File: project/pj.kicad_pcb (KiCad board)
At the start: 2 copper layers, 65 x 56.5 mm, 19 parts, among them J1 RPi_GPIO, J10 Pico PWR enable, J12 Conn_01x16_Pin, J2 2B+, J3 zero, J4 3A+, J5 3B+, J6 4, J7 Conn_01x02, J8 Conn_01x02, J9 External PWR, SW1 SW_Push, SW2 SW_Push

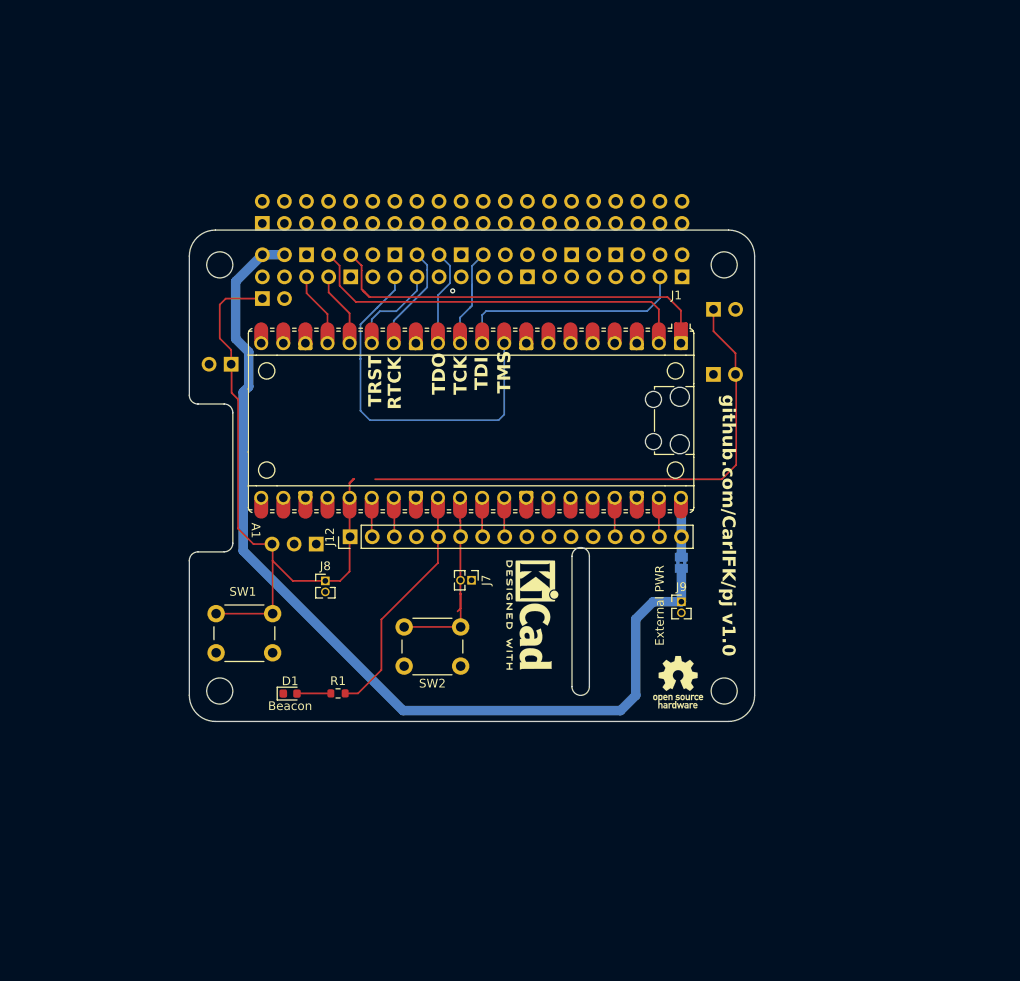
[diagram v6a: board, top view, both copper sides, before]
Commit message: ground plane, reroute some reset
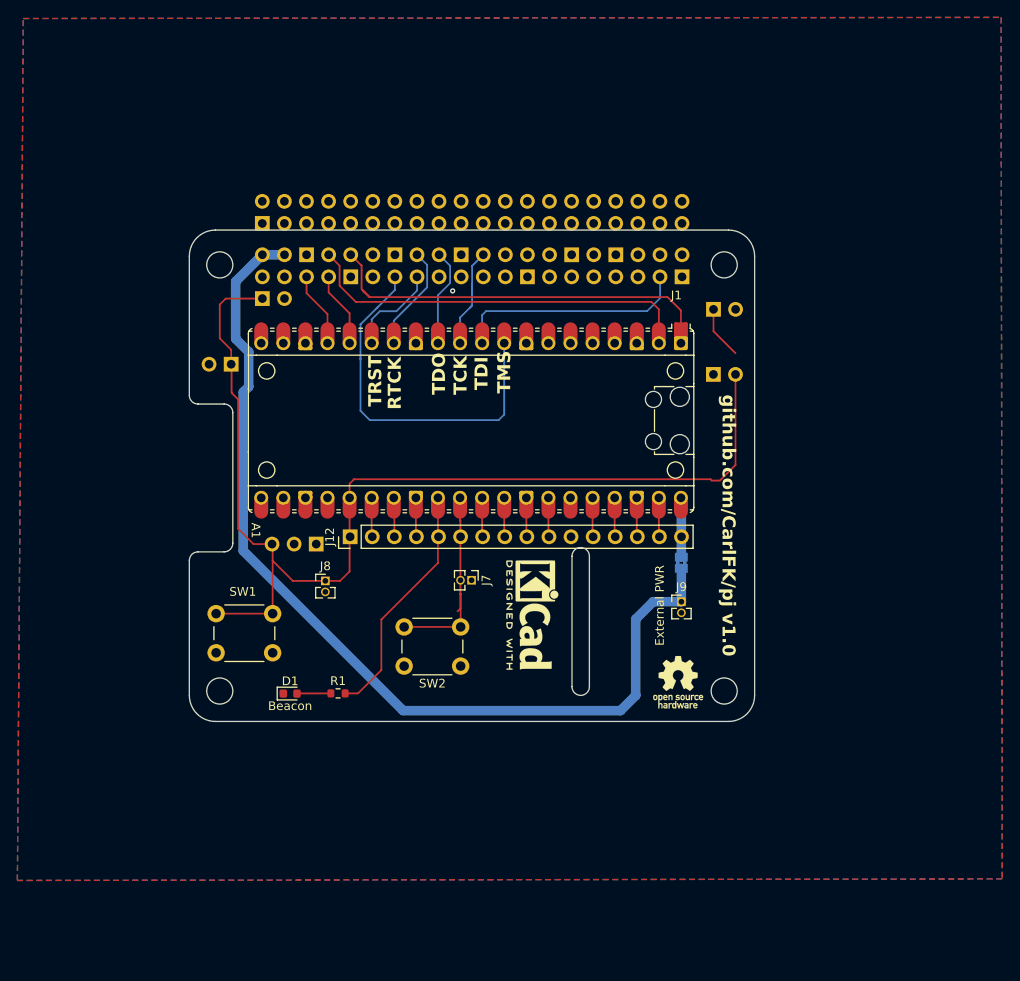
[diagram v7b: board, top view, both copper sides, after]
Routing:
- net unconnected-(J4-Pin_1-Pad1): track 61.1 -> 6.10 mm
- net Net-(A1-GPIO19): track 72.8 -> 127.1 mm
- net GND: track 0.19 -> 9.20 mm
- net Net-(A1-GPIO28_ADC2): track 0.00 -> 4.51 mm
- net Net-(A1-AGND): track 0.00 -> 4.51 mm
- net Net-(A1-3V3): track 0.00 -> 4.51 mm
- added copper zone on B.Cu, net GND
- added copper zone on F.Cu, net GND
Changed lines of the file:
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@@
 		(fp_arc
 			(start 10.579676 25.189937)
-			(mid 10.35796 25.493961)
+			(mid 10.357949 25.493953)
 			(end 10 25.61)
 			(stroke
@@
 		)
 		(property "Value" "3B+"
-			(at 0 -4.87 90)
-			(layer "B.Fab")
+			(at -2 -2.61 0)
+			(layer "F.Fab")
 			(effects
 				(font
@@
 					(thickness 0.15)
 				)
-				(justify mirror)
 			)
 		)
@@
 		)
 		(property "Value" "3A+"
-			(at 0 -4.87 90)
-			(layer "B.Fab")
+			(at 2 -0.13 0)
+			(layer "F.Fab")
 			(effects
 				(font
@@
 					(thickness 0.15)
 				)
-				(justify mirror)
 			)
 		)
@@
 		(net 10)
 	)
+	(segment
+		(start 62.4675 71.28)
+		(end 62.4675 75.6975)
+		(width 0.2)
+		(layer "F.Cu")
+		(net 11)
+	)
+	(segment
+		(start 62.4675 75.6975)
+		(end 62.53 75.76)
+		(width 0.2)
+		(layer "F.Cu")
+		(net 11)
+	)
+	(segment
+		(start 87.8675 75.6975)
+		(end 87.93 75.76)
+		(width 0.2)
+		(layer "F.Cu")
+		(net 11)
+	)
+	(segment
+		(start 87.8675 71.28)
+		(end 87.8675 75.6975)
+		(width 0.2)
+		(layer "F.Cu")
+		(net 11)
+	)
 	(via
 		(at 66.7 47.49)
@@
 	)
 	(segment
-		(start 44.82 48.37)
-		(end 40.61 48.37)
+		(start 96.336278 69.146278)
+		(end 55.363722 69.146278)
 		(width 0.2)
 		(layer "F.Cu")
@@
 	)
 	(segment
-		(start 42.02 74.82)
-		(end 43.8 76.6)
+		(start 44.82 48.37)
+		(end 40.61 48.37)
 		(width 0.2)
 		(layer "F.Cu")
@@
 	)
 	(segment
-		(start 54.8475 71.28)
-		(end 54.8475 69.6325)
+		(start 42.02 74.82)
+		(end 43.8 76.6)
 		(width 0.2)
 		(layer "F.Cu")
@@
 	)
 	(segment
-		(start 55.38 69.1)
-		(end 55.28 69.1)
+		(start 54.8475 69.6625)
+		(end 55.3 69.21)
 		(width 0.2)
 		(layer "F.Cu")
@@
 	)
 	(segment
-		(start 54.8475 69.6325)
-		(end 55.38 69.1)
+		(start 99.22 57.09)
+		(end 99.22 67.51)
 		(width 0.2)
 		(layer "F.Cu")
@@
 	)
 	(segment
+		(start 54.8475 71.28)
+		(end 54.8475 69.6625)
+		(width 0.2)
+		(layer "F.Cu")
+		(net 13)
+	)
+	(segment
 		(start 46 76.67)
 		(end 45.93 76.6)
@@
 	)
 	(segment
+		(start 99.22 67.51)
+		(end 97.43 69.3)
+		(width 0.2)
+		(layer "F.Cu")
+		(net 13)
+	)
+	(segment
+		(start 55.363722 69.146278)
+		(end 55.3 69.21)
+		(width 0.2)
+		(layer "F.Cu")
+		(net 13)
+	)
+	(segment
 		(start 52.06 79.18)
 		(end 52.11 79.13)
@@
 	)
 	(segment
-		(start 55.28 69.1)
-		(end 54.81 69.57)
+		(start 96.49 69.3)
+		(end 96.336278 69.146278)
 		(width 0.2)
 		(layer "F.Cu")
@@
 	)
 	(segment
+		(start 97.43 69.3)
+		(end 96.49 69.3)
+		(width 0.2)
+		(layer "F.Cu")
+		(net 13)
+	)
+	(segment
 		(start 46 78.51)
 		(end 46 76.67)
@@
 	)
 	(segment
+		(start 82.7875 75.6975)
+		(end 82.85 75.76)
+		(width 0.2)
+		(layer "F.Cu")
+		(net 15)
+	)
+	(segment
+		(start 82.7875 71.28)
+		(end 82.7875 75.6975)
+		(width 0.2)
+		(layer "F.Cu")
+		(net 15)
+	)
+	(segment
 		(start 93 71.3325)
 		(end 92.9475 71.28)
@@
 	)
 	(segment
+		(start 75.1675 71.28)
+		(end 75.1675 75.6975)
+		(width 0.2)
+		(layer "F.Cu")
+		(net 17)
+	)
+	(segment
+		(start 75.1675 75.6975)
+		(end 75.23 75.76)
+		(width 0.2)
+		(layer "F.Cu")
+		(net 17)
+	)
+	(segment
 		(start 70.0875 50.2725)
 		(end 70.55 49.81)
@@
 	)
 	(segment
+		(start 77.7075 71.28)
+		(end 77.7075 75.6975)
+		(width 0.2)
+		(layer "F.Cu")
+		(net 23)
+	)
+	(segment
+		(start 77.7075 75.6975)
+		(end 77.77 75.76)
+		(width 0.2)
+		(layer "F.Cu")
+		(net 23)
+	)
+	(segment
 		(start 60.22 49.83)
 		(end 62.6 47.45)
@@
 	)
 	(segment
-		(start 99.29 57.09)
-		(end 99.3 57.1)
-		(width 0.2)
-		(layer "F.Cu")
-		(net 29)
-	)
-	(segment
-		(start 99.22 54.66)
-		(end 99.22 57.09)
-		(width 0.2)
-		(layer "F.Cu")
-		(net 29)
-	)
-	(segment
-		(start 57.783778 69.146278)
-		(end 97.653722 69.146278)
-		(width 0.2)
-		(layer "F.Cu")
-		(net 29)
-	)
-	(segment
-		(start 97.653722 69.146278)
-		(end 99.3 67.5)
-		(width 0.2)
-		(layer "F.Cu")
-		(net 29)
-	)
-	(segment
-		(start 99.3 57.1)
-		(end 99.3 67.5)
-		(width 0.2)
-		(layer "F.Cu")
-		(net 29)
-	)
-	(segment
 		(start 96.69 49.61)
 		(end 96.69 52.13)
@@
 		(net 58)
 	)
+	(zone
+		(net 11)
+		(net_name "GND")
+		(layers "F&B.Cu")
+		(hatch edge 0.5)
+		(connect_pads
+			(clearance 0.5)
+		)
+		(min_thickness 0.25)
+		(filled_areas_thickness no)
+		(fill yes
+			(thermal_gap 0.5)
+			(thermal_bridge_width 0.5)
+		)
+		(polygon
+			(pts
+				(xy 17.33 16.17) (xy 129.76 16.04) (xy 129.89 115.1) (xy 16.65 115.28)
+			)
+		)
+	)
 )

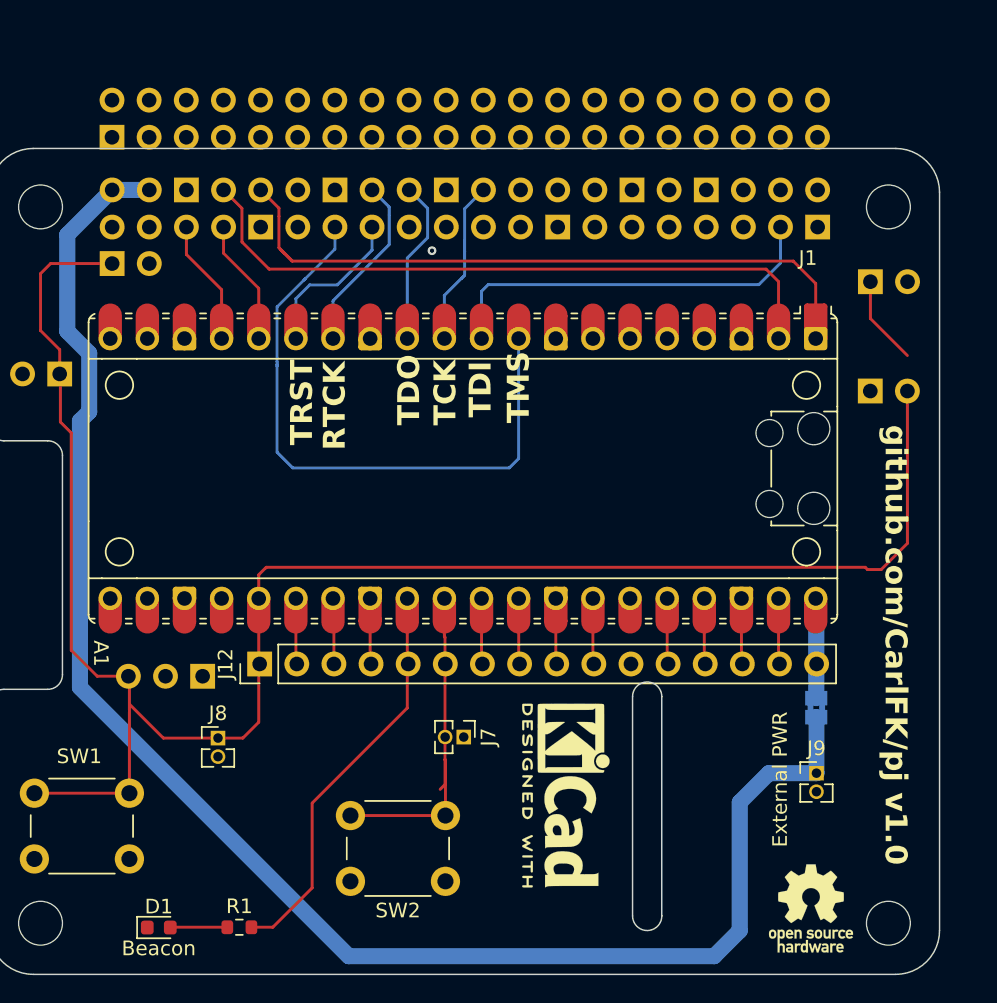
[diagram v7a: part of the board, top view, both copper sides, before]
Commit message: add missing connection to hole.
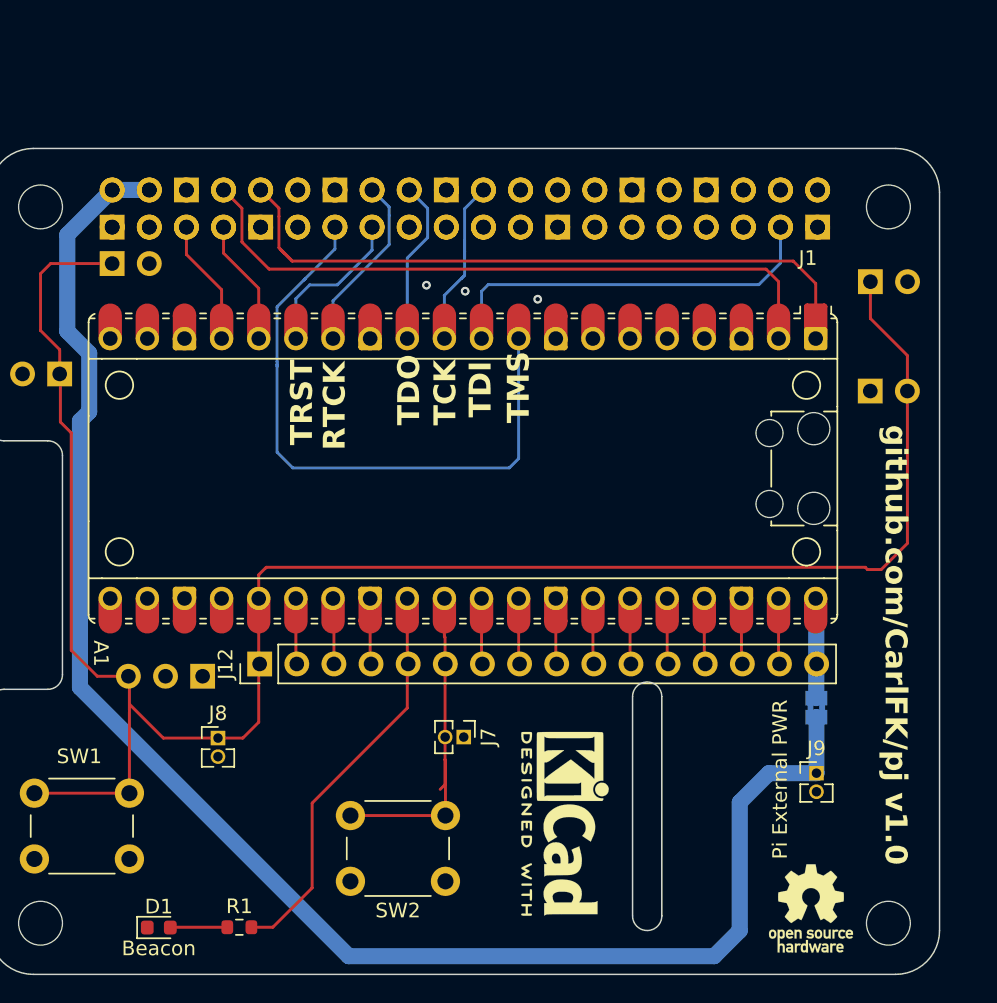
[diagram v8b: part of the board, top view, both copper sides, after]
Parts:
- J10: value Pico PWR enable -> Pi PWR enable
- J6: value 4 -> Pi 4
- J7: value Conn_01x02 -> Reset Pico
- J8: value Conn_01x02 -> Reset Pi
- J9: value External PWR -> Pi External PWR
- SW1: value SW_Push -> Reset Pi
- SW2: value SW_Push -> Reset Pico
- moved REF** 6.15 mm to (44.8, 45.9)
- moved REF** 1.93 mm to (75.8, 86.7)
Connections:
- J4 pad 1: unconnected-(J4-Pin_1-Pad1) -> Net-(A1-GPIO19)
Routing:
- net Net-(A1-GPIO19): track 127.1 -> 135.6 mm
- net unconnected-(J4-Pin_1-Pad1): track 6.10 -> 0.00 mm
- net Net-(A1-ADC_VREF): track 0.00 -> 4.51 mm
- net GND: vias 1 -> 3
